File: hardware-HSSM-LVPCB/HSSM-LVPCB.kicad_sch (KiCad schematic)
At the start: 67 parts, among them J1 UFL_R_SMT_1_10, J2 CONN_MINITEK127_10P_20021112-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, Q1 Q_MOSFET_N_BSS123, Q2 Q_MOSFET_N_BSS123, SW1 SW_TACT_SKRPACE010, SW2 SW_TACT_SKRPACE010, SW3 SW_TACT_SKRPACE010, SW4 SW_TACT_SKRPACE010, U1 ESP32-C6, U2 W25Q64JVSSIQ_SOIC-8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

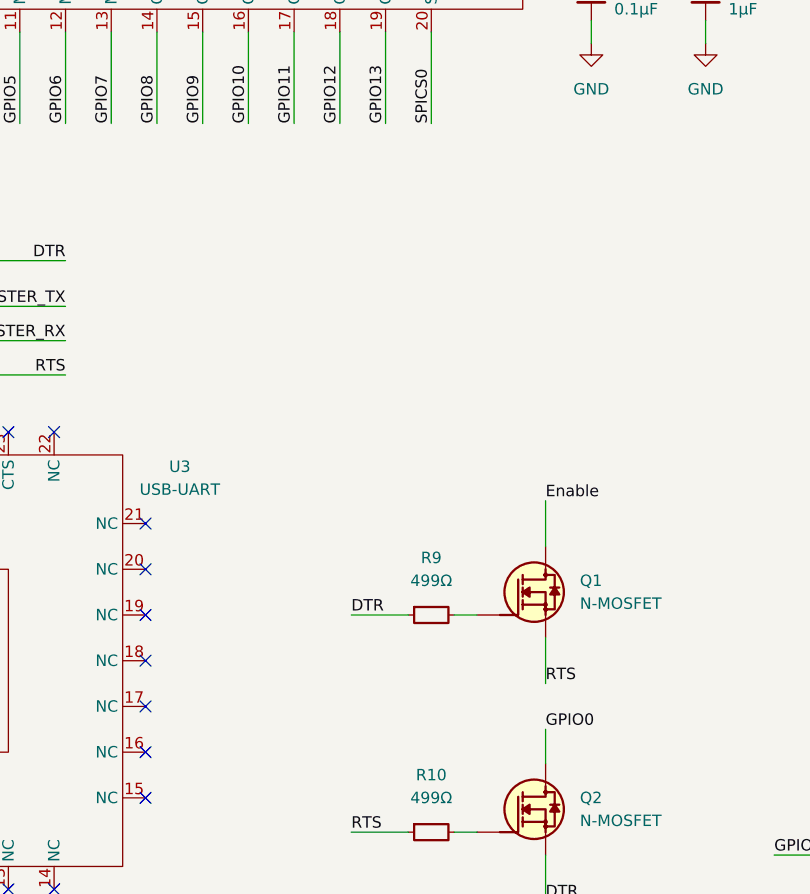
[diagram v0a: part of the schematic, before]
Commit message: [#4] Add FFC_solder_connector_16pos
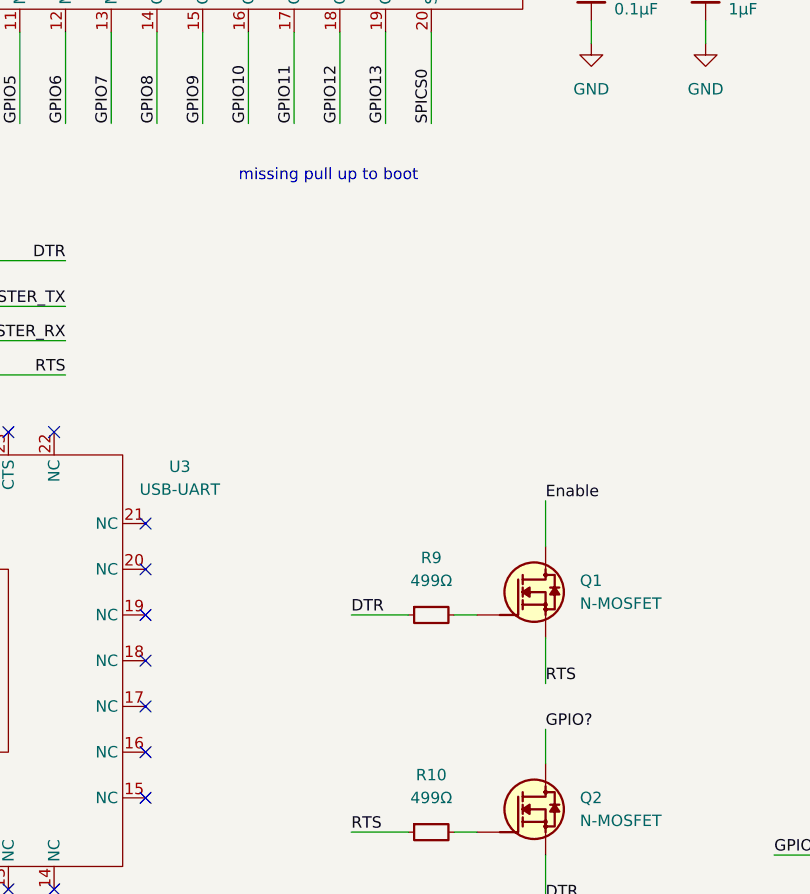
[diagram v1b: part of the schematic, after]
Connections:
- net GPIO0: no longer Q2.3 (D)
- net GPIO?: now also Q2.3 (D)
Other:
- note added: "missing pull up to boot"
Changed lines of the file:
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@@
+		)
+	)
+	(text "missing pull up to boot\n"
+		(exclude_from_sim no)
+		(at 151.13 170.942 0)
+		(effects
+			(font
+				(size 1.27 1.27)
+			)
 		)
 	)
@@
 		)
 	)
-	(label "GPIO0"
+	(label "GPIO?"
 		(at 175.26 232.41 0)
 		(fields_autoplaced yes)

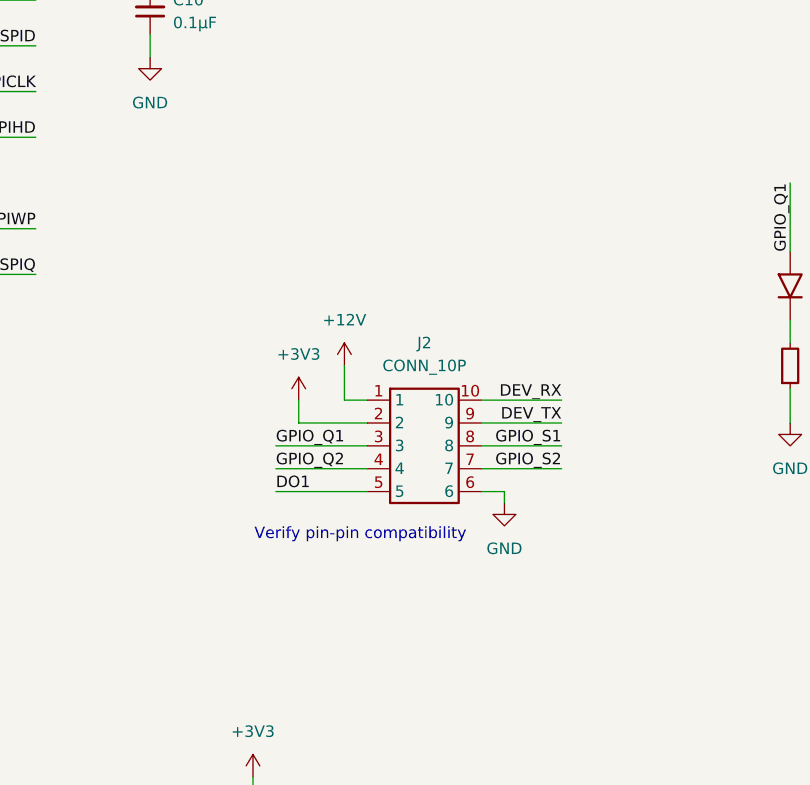
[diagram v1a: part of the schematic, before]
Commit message: [#4] Replace board-to-board connector
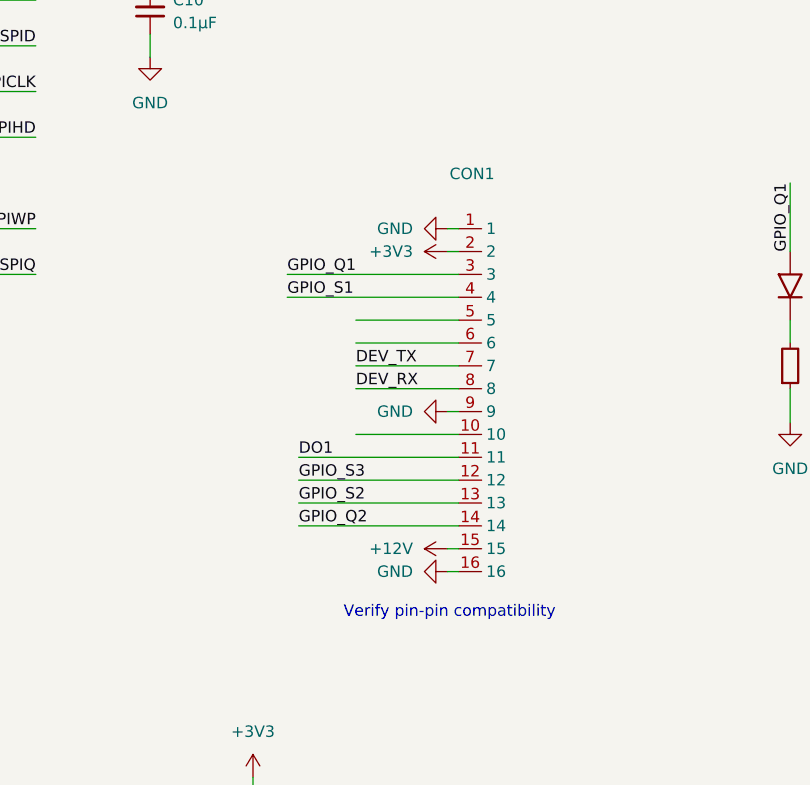
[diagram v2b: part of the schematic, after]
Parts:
- removed J2: CONN_MINITEK127_10P_20021112-00010T1LF, HSSM-LVPCB:MINITEK127_10P, symbol HSSM-LVPCB:CONN_MINITEK127_10P_20021112-00010T1LF
- added CON1: ~, symbol HSSM-LVPCB:FFC_solder_connector_16pos
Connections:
- net +12V: now also CON1.15
- net +3V3: now also CON1.2
- net DEV_RX: now also CON1.8
- net DEV_TX: now also CON1.7
- net DO1: now also CON1.11
- net GND: now also CON1.1, CON1.16, CON1.9
- net GPIO_Q1: now also CON1.3
- net GPIO_Q2: now also CON1.14
- net GPIO_S1: now also CON1.4
- net GPIO_S2: now also CON1.13
- net GPIO_S3: now also CON1.12

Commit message: [#8] Add CONMHF1-SMD-T
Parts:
- J1: footprint HSSM-LVPCB:UFL_SMT_Footprint -> HSSM-LVPCB:CONMHF1-SMD-T
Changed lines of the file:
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@@
 			)
 		)
-		(property "Footprint" "HSSM-LVPCB:UFL_SMT_Footprint"
+		(property "Footprint" "HSSM-LVPCB:CONMHF1-SMD-T"
 			(at 29.21 92.964 0)
 			(effects

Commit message: [#8] Add Bosch_LGA-8_2.5x2.5mm_P0.65mm_ClockwisePinNumbering
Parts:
- U4: footprint HSSM-LVPCB:U_LGA_2.5x2.5 -> HSSM-LVPCB:Bosch_LGA-8_2.5x2.5mm_P0.65mm_ClockwisePinNumbering
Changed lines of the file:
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@@
 			)
 		)
-		(property "Footprint" "HSSM-LVPCB:U_LGA_2.5x2.5"
+		(property "Footprint" "HSSM-LVPCB:Bosch_LGA-8_2.5x2.5mm_P0.65mm_ClockwisePinNumbering"
 			(at 282.194 92.71 0)
 			(effects

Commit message: [#8] Add L 0402
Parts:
- C10, C11, C15, C16, C17, C18, C19, C20, C21, C3, C4, C7, C8: footprint HSSM-HVPCB:C_0402 -> HSSM-LVPCB:C_0402
- C12, C5, C9: footprint HSSM-HVPCB:C_0603 -> HSSM-LVPCB:C_0603
- D2, D3, D4, D5, D6: footprint LED_SMD:LED_1608_0603Metric -> HSSM-LVPCB:LED_0603_1608Metric
- J1: footprint HSSM-LVPCB:CONMHF1-SMD-T -> HSSM-LVPCB:UFL_SMT_Footprint
- L2: footprint HSSM-HVPCB:L_0402 -> HSSM-LVPCB:L_0402
- R1, R10, R14, R15, R16, R17, R18, R19, R2, R20, R21, R22, R3, R4, R5, R6, R7, R8, R9: footprint HSSM-HVPCB:R_0402 -> HSSM-LVPCB:R_0402
- U1: footprint HSSM-LVPCB:ESP32-C6 -> HSSM-LVPCB:QFN-40-1EP_5x5mm_P0.4mm_EP3.6x3.6mm
- U2: footprint HSSM-LVPCB:SOIC-8 -> HSSM-LVPCB:SOIC-8_3.9x4.9mm_P1.27mm
- U5: footprint HSSM-LVPCB:U_LGA_3.3x3.3 -> HSSM-LVPCB:XDCR_ENS160-BGLM
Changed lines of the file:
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@@
 			)
 		)
-		(property "Footprint" "HSSM-HVPCB:C_0603"
+		(property "Footprint" "HSSM-LVPCB:C_0603"
 			(at 159.004 54.61 0)
 			(effects
@@
 			)
 		)
-		(property "Footprint" "HSSM-HVPCB:C_0603"
+		(property "Footprint" "HSSM-LVPCB:C_0603"
 			(at 203.454 151.13 0)
 			(effects
@@
 			)
 		)
-		(property "Footprint" "LED_SMD:LED_1608_0603Metric"
+		(property "Footprint" "HSSM-LVPCB:LED_0603_1608Metric"
 			(at 338.074 143.51 0)
 			(effects
@@
 			)
 		)
-		(property "Footprint" "HSSM-HVPCB:R_0402"
+		(property "Footprint" "HSSM-LVPCB:R_0402"
 			(at 200.914 34.29 0)
 			(effects
@@
 			)
 		)
-		(property "Footprint" "HSSM-HVPCB:R_0402"
+		(property "Footprint" "HSSM-LVPCB:R_0402"
 			(at 186.69 147.574 0)
 			(effects
@@
 			)
 		)
-		(property "Footprint" "HSSM-HVPCB:C_0402"
+		(property "Footprint" "HSSM-LVPCB:C_0402"
 			(at 147.574 54.61 0)
 			(effects
@@
 			)
 		)
-		(property "Footprint" "HSSM-HVPCB:C_0402"
+		(property "Footprint" "HSSM-LVPCB:C_0402"
 			(at 291.084 224.79 0)
 			(effects
@@
 			)
 		)
-		(property "Footprint" "HSSM-HVPCB:R_0402"
+		(property "Footprint" "HSSM-LVPCB:R_0402"
 			(at 186.69 127.254 0)
 			(effects
@@
 			)
 		)
-		(property "Footprint" "HSSM-HVPCB:R_0402"
+		(property "Footprint" "HSSM-LVPCB:R_0402"
 			(at 338.074 152.4 0)
 			(effects
@@
 			)
 		)
-		(property "Footprint" "HSSM-HVPCB:R_0402"
+		(property "Footprint" "HSSM-LVPCB:R_0402"
 			(at 96.52 59.436 0)
 			(effects
@@
 			)
 		)
-		(property "Footprint" "HSSM-HVPCB:C_0402"
+		(property "Footprint" "HSSM-LVPCB:C_0402"
 			(at 61.214 113.03 0)
 			(effects
@@
 			)
 		)
-		(property "Footprint" "HSSM-HVPCB:R_0402"
+		(property "Footprint" "HSSM-LVPCB:R_0402"
 			(at 194.31 152.654 0)
 			(effects
@@
 			)
 		)
-		(property "Footprint" "HSSM-HVPCB:C_0402"
+		(property "Footprint" "HSSM-LVPCB:C_0402"
 			(at 90.424 120.65 0)
 			(effects
@@
 			)
 		)
-		(property "Footprint" "HSSM-LVPCB:CONMHF1-SMD-T"
+		(property "Footprint" "HSSM-LVPCB:UFL_SMT_Footprint"
 			(at 29.21 92.964 0)
 			(effects
@@
 			)
 		)
-		(property "Footprint" "HSSM-LVPCB:SOIC-8"
+		(property "Footprint" "HSSM-LVPCB:SOIC-8_3.9x4.9mm_P1.27mm"
 			(at 205.74 61.214 0)
 			(effects
@@
 			)
 		)
-		(property "Footprint" "HSSM-HVPCB:R_0402"
+		(property "Footprint" "HSSM-LVPCB:R_0402"
 			(at 291.084 213.36 0)
 			(effects
@@
 			)
 		)
-		(property "Footprint" "HSSM-HVPCB:C_0402"
+		(property "Footprint" "HSSM-LVPCB:C_0402"
 			(at 190.754 151.13 0)
 			(effects
@@
 			)
 		)
-		(property "Footprint" "LED_SMD:LED_1608_0603Metric"
+		(property "Footprint" "HSSM-LVPCB:LED_0603_1608Metric"
 			(at 312.674 143.51 0)
 			(effects
@@
 			)
 		)
-		(property "Footprint" "HSSM-LVPCB:U_LGA_3.3x3.3"
+		(property "Footprint" "HSSM-LVPCB:XDCR_ENS160-BGLM"
 			(at 377.19 92.71 0)
 			(effects
@@
 			)
 		)
-		(property "Footprint" "HSSM-HVPCB:C_0402"
+		(property "Footprint" "HSSM-LVPCB:C_0402"
 			(at 82.804 245.11 0)
 			(effects
@@
 			)
 		)
-		(property "Footprint" "HSSM-HVPCB:R_0402"
+		(property "Footprint" "HSSM-LVPCB:R_0402"
 			(at 162.56 254.254 0)
 			(effects
@@
 			)
 		)
-		(property "Footprint" "LED_SMD:LED_1608_0603Metric"
+		(property "Footprint" "HSSM-LVPCB:LED_0603_1608Metric"
 			(at 325.374 143.51 0)
 			(effects
@@
 			)
 		)
-		(property "Footprint" "HSSM-HVPCB:R_0402"
+		(property "Footprint" "HSSM-LVPCB:R_0402"
 			(at 194.31 132.334 0)
 			(effects
@@
 			)
 		)
-		(property "Footprint" "HSSM-HVPCB:C_0402"
+		(property "Footprint" "HSSM-LVPCB:C_0402"
 			(at 227.584 113.03 0)
 			(effects
@@
 			)
 		)
-		(property "Footprint" "LED_SMD:LED_1608_0603Metric"
+		(property "Footprint" "HSSM-LVPCB:LED_0603_1608Metric"
 			(at 350.774 143.51 0)
 			(effects
@@
 			)
 		)
-		(property "Footprint" "HSSM-HVPCB:R_0402"
+		(property "Footprint" "HSSM-LVPCB:R_0402"
 			(at 325.374 152.4 0)
 			(effects
@@
 			)
 		)
-		(property "Footprint" "HSSM-HVPCB:C_0402"
+		(property "Footprint" "HSSM-LVPCB:C_0402"
 			(at 233.426 69.85 0)
 			(effects
@@
 			)
 		)
-		(property "Footprint" "HSSM-HVPCB:R_0402"
+		(property "Footprint" "HSSM-LVPCB:R_0402"
 			(at 219.964 240.03 0)
 			(effects
@@
 			)
 		)
-		(property "Footprint" "HSSM-HVPCB:R_0402"
+		(property "Footprint" "HSSM-LVPCB:R_0402"
 			(at 162.56 230.124 0)
 			(effects
@@
 			)
 		)
-		(property "Footprint" "HSSM-HVPCB:C_0402"
+		(property "Footprint" "HSSM-LVPCB:C_0402"
 			(at 377.444 224.79 0)
 			(effects
@@
 			)
 		)
-		(property "Footprint" "HSSM-HVPCB:C_0603"
+		(property "Footprint" "HSSM-LVPCB:C_0603"
 			(at 51.054 113.03 0)
 			(effects
@@
 			)
 		)
-		(property "Footprint" "HSSM-HVPCB:R_0402"
+		(property "Footprint" "HSSM-LVPCB:R_0402"
 			(at 336.804 213.36 0)
 			(effects
@@
 			)
 		)
-		(property "Footprint" "HSSM-HVPCB:R_0402"
+		(property "Footprint" "HSSM-LVPCB:R_0402"
 			(at 377.444 213.36 0)
 			(effects
@@
 			)
 		)
-		(property "Footprint" "HSSM-HVPCB:L_0402"
+		(property "Footprint" "HSSM-LVPCB:L_0402"
 			(at 58.42 117.094 0)
 			(effects
@@
 			)
 		)
-		(property "Footprint" "HSSM-LVPCB:ESP32-C6"
+		(property "Footprint" "HSSM-LVPCB:QFN-40-1EP_5x5mm_P0.4mm_EP3.6x3.6mm"
 			(at 139.765 177.579 0)
 			(effects
@@
 			)
 		)
-		(property "Footprint" "HSSM-HVPCB:C_0402"
+		(property "Footprint" "HSSM-LVPCB:C_0402"
 			(at 265.684 80.01 0)
 			(effects
@@
 			)
 		)
-		(property "Footprint" "HSSM-HVPCB:R_0402"
+		(property "Footprint" "HSSM-LVPCB:R_0402"
 			(at 312.674 152.4 0)
 			(effects
@@
 			)
 		)
-		(property "Footprint" "HSSM-HVPCB:R_0402"
+		(property "Footprint" "HSSM-LVPCB:R_0402"
 			(at 186.69 137.414 0)
 			(effects
@@
 			)
 		)
-		(property "Footprint" "HSSM-HVPCB:R_0402"
+		(property "Footprint" "HSSM-LVPCB:R_0402"
 			(at 298.704 152.4 0)
 			(effects
@@
 			)
 		)
-		(property "Footprint" "HSSM-HVPCB:R_0402"
+		(property "Footprint" "HSSM-LVPCB:R_0402"
 			(at 350.774 152.4 0)
 			(effects
@@
 			)
 		)
-		(property "Footprint" "HSSM-HVPCB:C_0402"
+		(property "Footprint" "HSSM-LVPCB:C_0402"
 			(at 76.454 113.03 0)
 			(effects
@@
 			)
 		)
-		(property "Footprint" "LED_SMD:LED_1608_0603Metric"
+		(property "Footprint" "HSSM-LVPCB:LED_0603_1608Metric"
 			(at 298.704 143.51 0)
 			(effects
@@
 			)
 		)
-		(property "Footprint" "HSSM-HVPCB:C_0402"
+		(property "Footprint" "HSSM-LVPCB:C_0402"
 			(at 219.964 251.46 0)
 			(effects
@@
 			)
 		)
-		(property "Footprint" "HSSM-HVPCB:R_0402"
+		(property "Footprint" "HSSM-LVPCB:R_0402"
 			(at 189.23 112.014 0)
 			(effects
@@
 			)
 		)
-		(property "Footprint" "HSSM-HVPCB:C_0402"
+		(property "Footprint" "HSSM-LVPCB:C_0402"
 			(at 336.804 224.79 0)
 			(effects

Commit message: [#8] Update symbols and import footprints to PCB
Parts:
- J1: footprint HSSM-LVPCB:UFL_SMT_Footprint -> HSSM-LVPCB:CONMHF1-SMD-T
- U3: footprint HSSM-LVPCB:QFN-28-EP -> HSSM-LVPCB:QFN-28-1EP_4x4mm_P0.4mm_EP2.3x2.3mm
- X1: footprint HSSM-LVPCB:X_2520 -> HSSM-LVPCB:ECS-2520SMV-400-FN-TR
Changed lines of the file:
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@@
 			)
 		)
-		(property "Footprint" "HSSM-LVPCB:QFN-28-EP"
+		(property "Footprint" "HSSM-LVPCB:QFN-28-1EP_4x4mm_P0.4mm_EP2.3x2.3mm"
 			(at 105.41 270.002 0)
 			(effects
@@
 			)
 		)
-		(property "Footprint" "HSSM-LVPCB:UFL_SMT_Footprint"
+		(property "Footprint" "HSSM-LVPCB:CONMHF1-SMD-T"
 			(at 29.21 92.964 0)
 			(effects
@@
 			)
 		)
-		(property "Footprint" "HSSM-LVPCB:X_2520"
+		(property "Footprint" "HSSM-LVPCB:ECS-2520SMV-400-FN-TR"
 			(at 96.52 68.834 0)
 			(effects

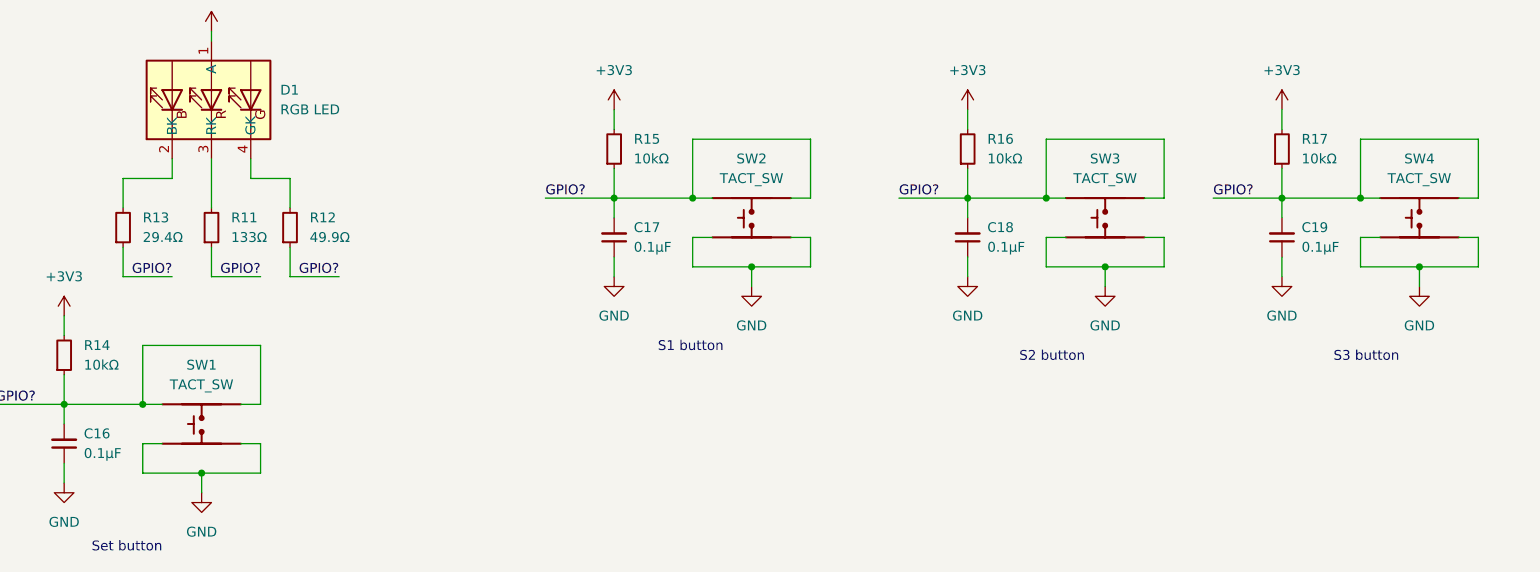
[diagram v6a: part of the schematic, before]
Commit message: [#9] Replace switches
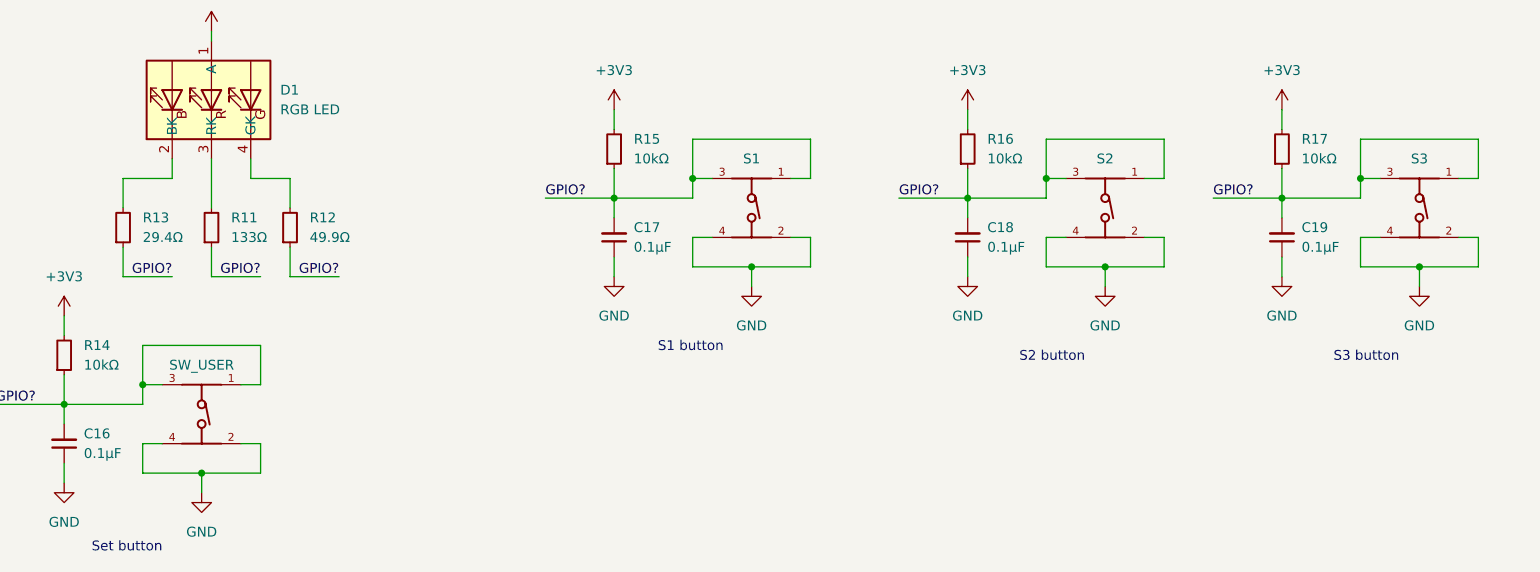
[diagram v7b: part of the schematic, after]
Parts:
- removed SW1, SW2, SW3, SW4: SW_TACT_SKRPACE010, HSSM-LVPCB:SW_TACT_SKRPACE010, symbol HSSM-LVPCB:SW_TACT_SKRPACE010
- added S1, S2, S3, SW_USER: 434331045822, HSSM-LVPCB:434331045822, symbol HSSM-LVPCB:SW_angle_434331045822
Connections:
- net GND: now also S1.2, S1.4, S2.2, S2.4, S3.2, S3.4, SW_USER.2, SW_USER.4
- net GPIO?: now also S1.1, S1.3, S2.1, S2.3, S3.1, S3.3, SW_USER.1, SW_USER.3
